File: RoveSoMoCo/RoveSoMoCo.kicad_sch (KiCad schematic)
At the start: 34 parts, among them Q1 SI4156DY, Q2 SI4156DY, Q3 SI4156DY, Q4 SI4156DY, U1 74LVC2G04, U2 IRS2005S, U3 IRS2005S, U4 74HC00

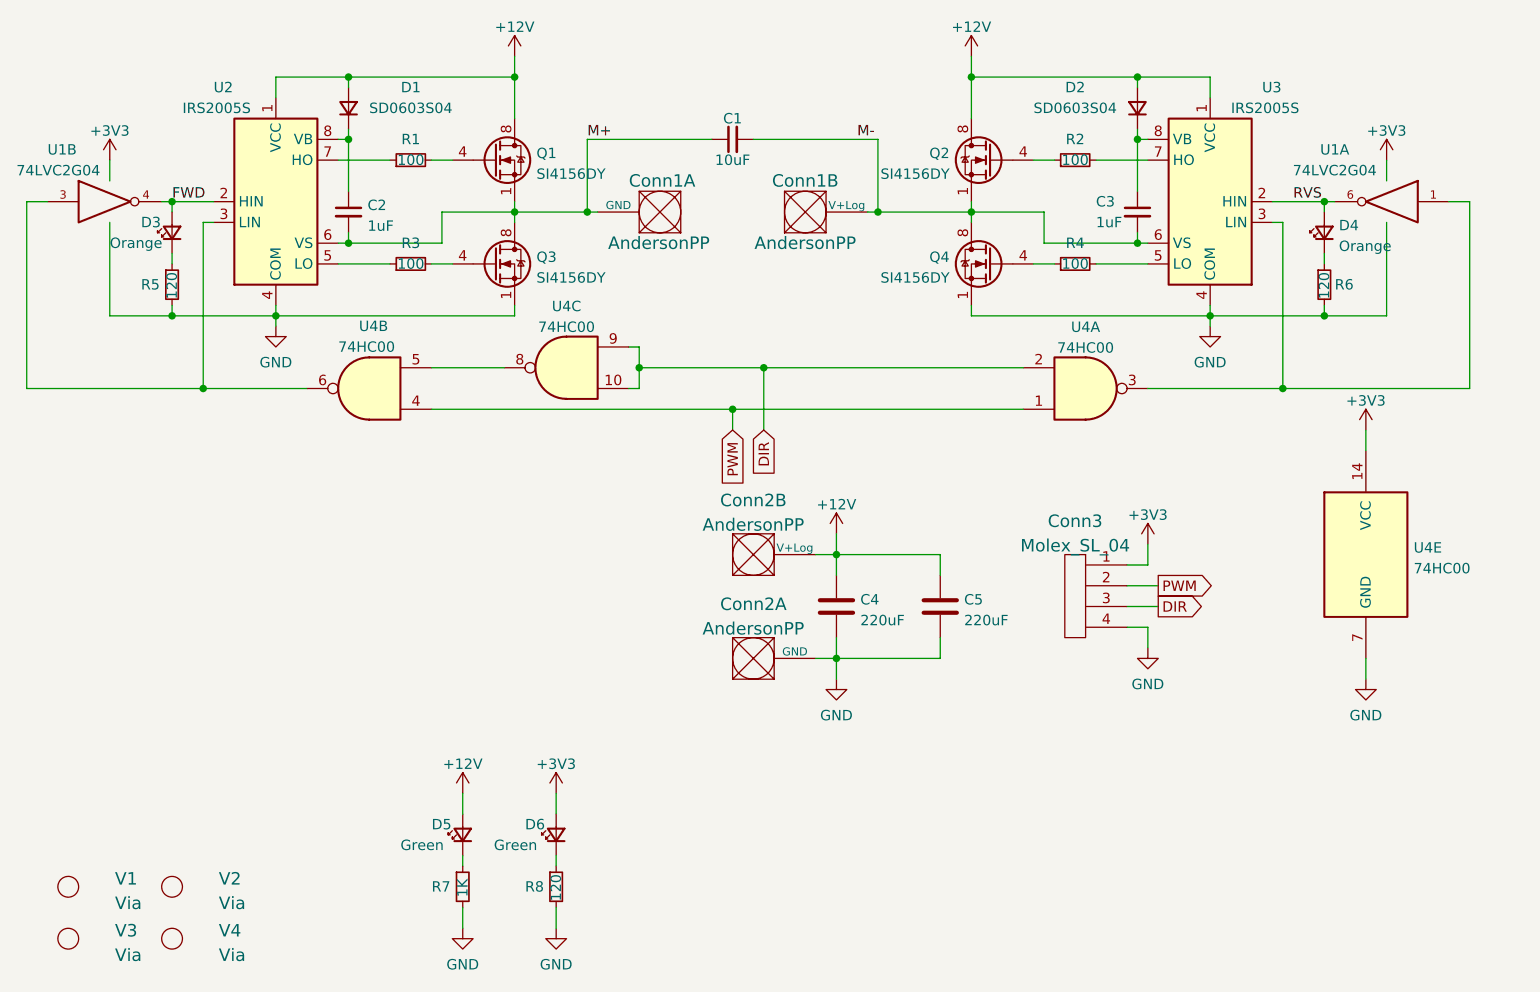
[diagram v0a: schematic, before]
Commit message: Switch to 4-layer
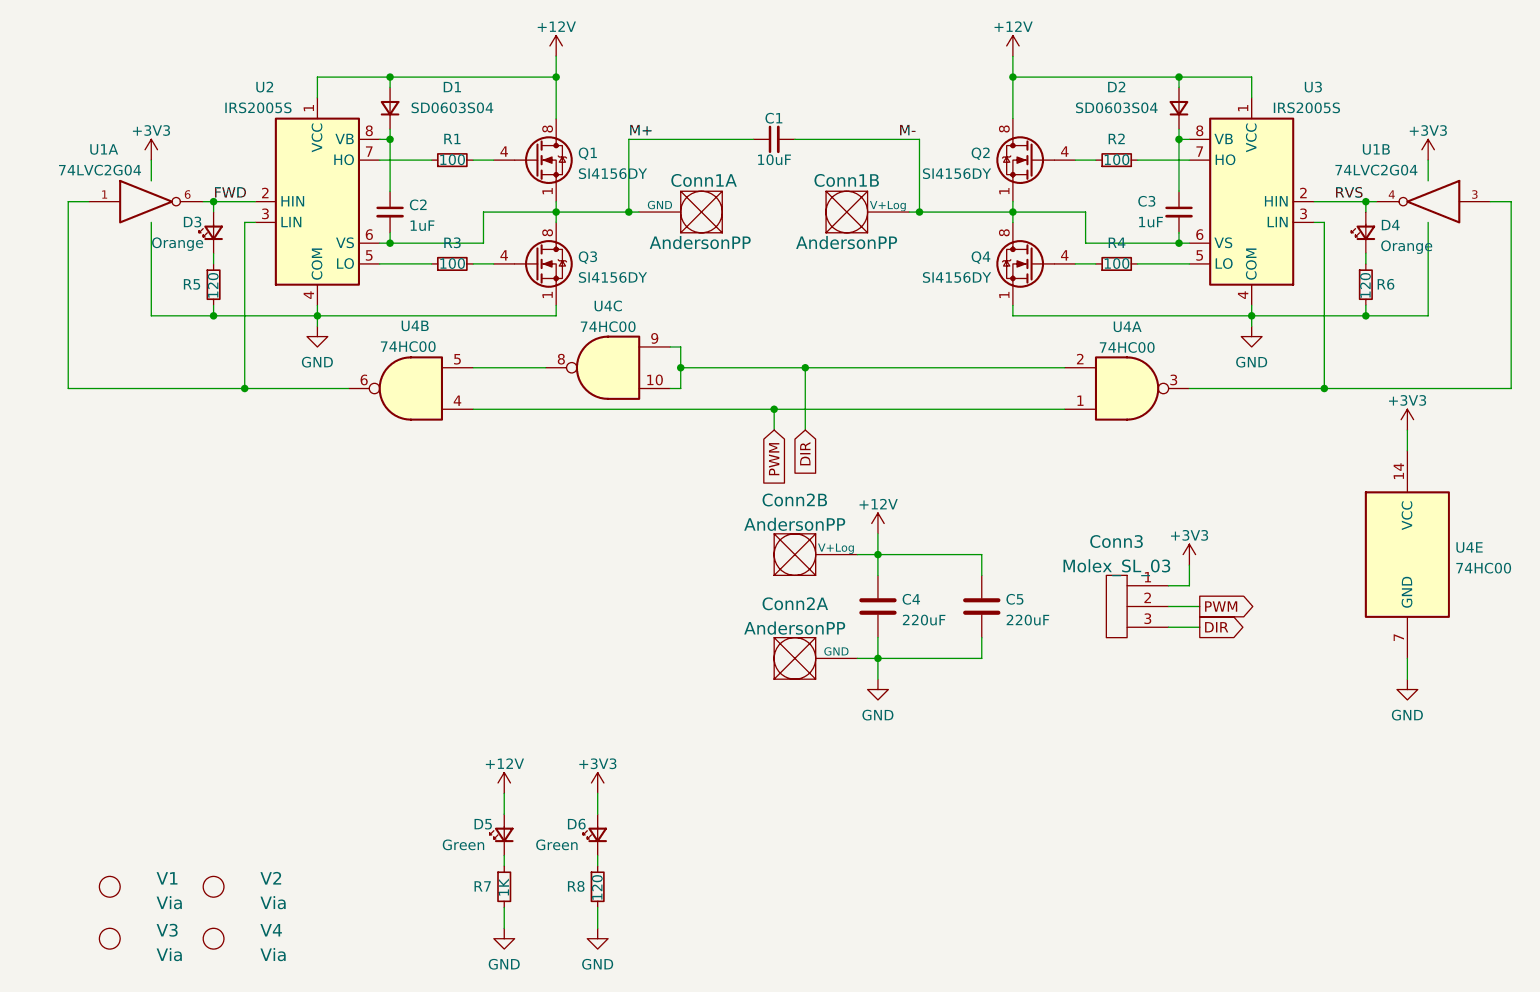
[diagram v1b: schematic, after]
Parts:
- removed Conn3: Molex_SL_04, MRDT_Connectors:MOLEX_SL_04_Vertical, symbol MRDT_Connectors:Molex_SL_04
- added Conn3: Molex_SL_03, MRDT_Connectors:MOLEX_SL_03_Vertical, symbol MRDT_Connectors:Molex_SL_03
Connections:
- net +3V3: now also Conn3.1
- net DIR: now also Conn3.3
- net FWD: now also U1.6; no longer U1.4
- net PWM: now also Conn3.2
- net RVS: now also U1.4; no longer U1.6
- net at U2.3 (LIN), U4.6: now also U1.1; no longer U1.3
- net at U3.3 (LIN), U4.3: now also U1.3; no longer U1.1

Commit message: Increased size of board and planes
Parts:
- D1, D2: footprint Diode_SMD:D_0201_0603Metric_Pad0.64x0.40mm_HandSolder -> Diode_SMD:D_0603_1608Metric_Pad1.05x0.95mm_HandSolder
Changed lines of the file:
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@@
     (property "Reference" "D2" (id 0) (at 147.32 24.13 90))
     (property "Value" "SD0603S04" (id 1) (at 147.32 26.67 90))
-    (property "Footprint" "Diode_SMD:D_0201_0603Metric_Pad0.64x0.40mm_HandSolder" (id 2) (at 154.94 26.67 90)
+    (property "Footprint" "Diode_SMD:D_0603_1608Metric_Pad1.05x0.95mm_HandSolder" (id 2) (at 154.94 26.67 90)
       (effects (font (size 1.27 1.27)) hide)
     )
@@
     (property "Reference" "D1" (id 0) (at 66.04 24.13 90))
     (property "Value" "SD0603S04" (id 1) (at 66.04 26.67 90))
-    (property "Footprint" "Diode_SMD:D_0201_0603Metric_Pad0.64x0.40mm_HandSolder" (id 2) (at 58.42 26.67 90)
+    (property "Footprint" "Diode_SMD:D_0603_1608Metric_Pad1.05x0.95mm_HandSolder" (id 2) (at 58.42 26.67 90)
       (effects (font (size 1.27 1.27)) hide)
     )
@@
     )
     (path "/d68d4f16-fd88-4ff9-a035-09ed3a2fb17b"
-      (reference "D1") (unit 1) (value "SD0603S04") (footprint "Diode_SMD:D_0201_0603Metric_Pad0.64x0.40mm_HandSolder")
+      (reference "D1") (unit 1) (value "SD0603S04") (footprint "Diode_SMD:D_0603_1608Metric_Pad1.05x0.95mm_HandSolder")
     )
     (path "/a537f83c-bd68-4c8b-a78b-5edb6f4ca3a1"
-      (reference "D2") (unit 1) (value "SD0603S04") (footprint "Diode_SMD:D_0201_0603Metric_Pad0.64x0.40mm_HandSolder")
+      (reference "D2") (unit 1) (value "SD0603S04") (footprint "Diode_SMD:D_0603_1608Metric_Pad1.05x0.95mm_HandSolder")
     )
     (path "/51ec69f2-127f-455e-8886-b0c918fbe4ff"
